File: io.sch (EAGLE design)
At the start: 53 parts, among them J1 SJ-3502-SMT-TR, Q1 2SCR574D3TL1, Q2 2SCR574D3TL1, U1 MCP1703T-5002E, U2 SA602AD8-SOIC, U3 LM386M-1, X1 Antenna, Y1 7.040MHz

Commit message: splitting boards, doing layouts
Split into two boards with jumpers between. Added jumper for crystal to be able to change reference frequency. Closer to real layouts, still need to solidify some parts.
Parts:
- removed C13: 47p, adafruit:C-USC0805
- removed C14: 220p, adafruit:C-USC0805
- removed C15: 0.1u, adafruit:C-USC0805
- removed C20, C21: 10n, adafruit:C-USC0805
- removed C26, C3: 33p, adafruit:C-USC0805
- removed C4: 270p, adafruit:C-USC0805
- removed D1, D2: 1N4148, adafruit:DIODE_SOD-123FL
- removed D3: MV2102, adafruit:DIODESOD-323F
- removed L1: 10uH, MLF2012E5R6KT000:MLF2012E5R6KT000
- removed L6: 18uH, MLF2012E5R6KT000:MLF2012E5R6KT000
- removed L7: 560uH, MLF2012E5R6KT000:MLF2012E5R6KT000
- removed L8: 5.6uH, MLF2012E5R6KT000:MLF2012E5R6KT000
- removed R1, R2: 1k, pot:TRIM_EU-3223G
- removed R3: 6.8k, adafruit:R-US_M0805
- removed U2: SA602AD8-SOIC, zort2:SA602AD8-SOIC
- removed VIN: AB9V, battery:AB9V
- removed Y1: 7.040MHz, adafruit:CRYSTALCTS406
- added JP1: (no value), adafruit:PINHD-2X4
- added U$2: 9V_968, zort2:9V_968
- L2: device MLF2012E5R6KT000:MLF2012E5R6KT000 -> Inductor:L_CHIP-1008(2520-METRIC)
- L4: device MLF2012E5R6KT000:MLF2012E5R6KT000 -> zort2:B966AS-160M-P3
- L5: device MLF2012E5R6KT000:MLF2012E5R6KT000 -> Inductor:L_CHIP-0805(2012-METRIC)
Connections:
- removed net N$1: C20.1, U2.IN_A
- removed net N$15: L6.2, Y1.1
- removed net N$16: C15.2, L6.1
- removed net N$17: C15.1, D3.C, L7.2
- removed net N$18: L7.1, R2.S
- removed net N$2: C21.1, U2.IN_B
- removed net N$3: C20.2, C26.1, C3.1, L1.2
- removed net N$4: C14.1, U2.OSC_B, Y1.2
- removed net N$5: C26.2, C3.2, C4.1, R1.S
- removed net N$6: L8.2, R1.E
- net 6V_DC: now also JP1.3; no longer R2.E, U2.VCC
- net ANT_IN: now also JP1.7; no longer D1.A, D2.C, L8.1
- net ANT_OUT: now also JP1.8; no longer C13.1, C14.2, R3.2, U2.OSC_E
- net GND: now also JP1.2, U$2.P$2; no longer C13.2, C21.2, C4.2, D1.C, D2.A, D3.A, L1.1, R1.A, R2.A, R3.1, U2.GND, VIN.-
- net OUT_A: now also JP1.5; no longer U2.OUT_A
- net OUT_B: now also JP1.6; no longer U2.OUT_B
- net VIN: now also JP1.1, U$2.P$1; no longer VIN.+
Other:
- note removed: "Input Attenuation"
- note removed: "RF Mixer"
- note removed: "VXO"
- moved on the sheet: C1, C10, C11, C12, C16, C17, C18, C19, C2, C22, C23, C24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

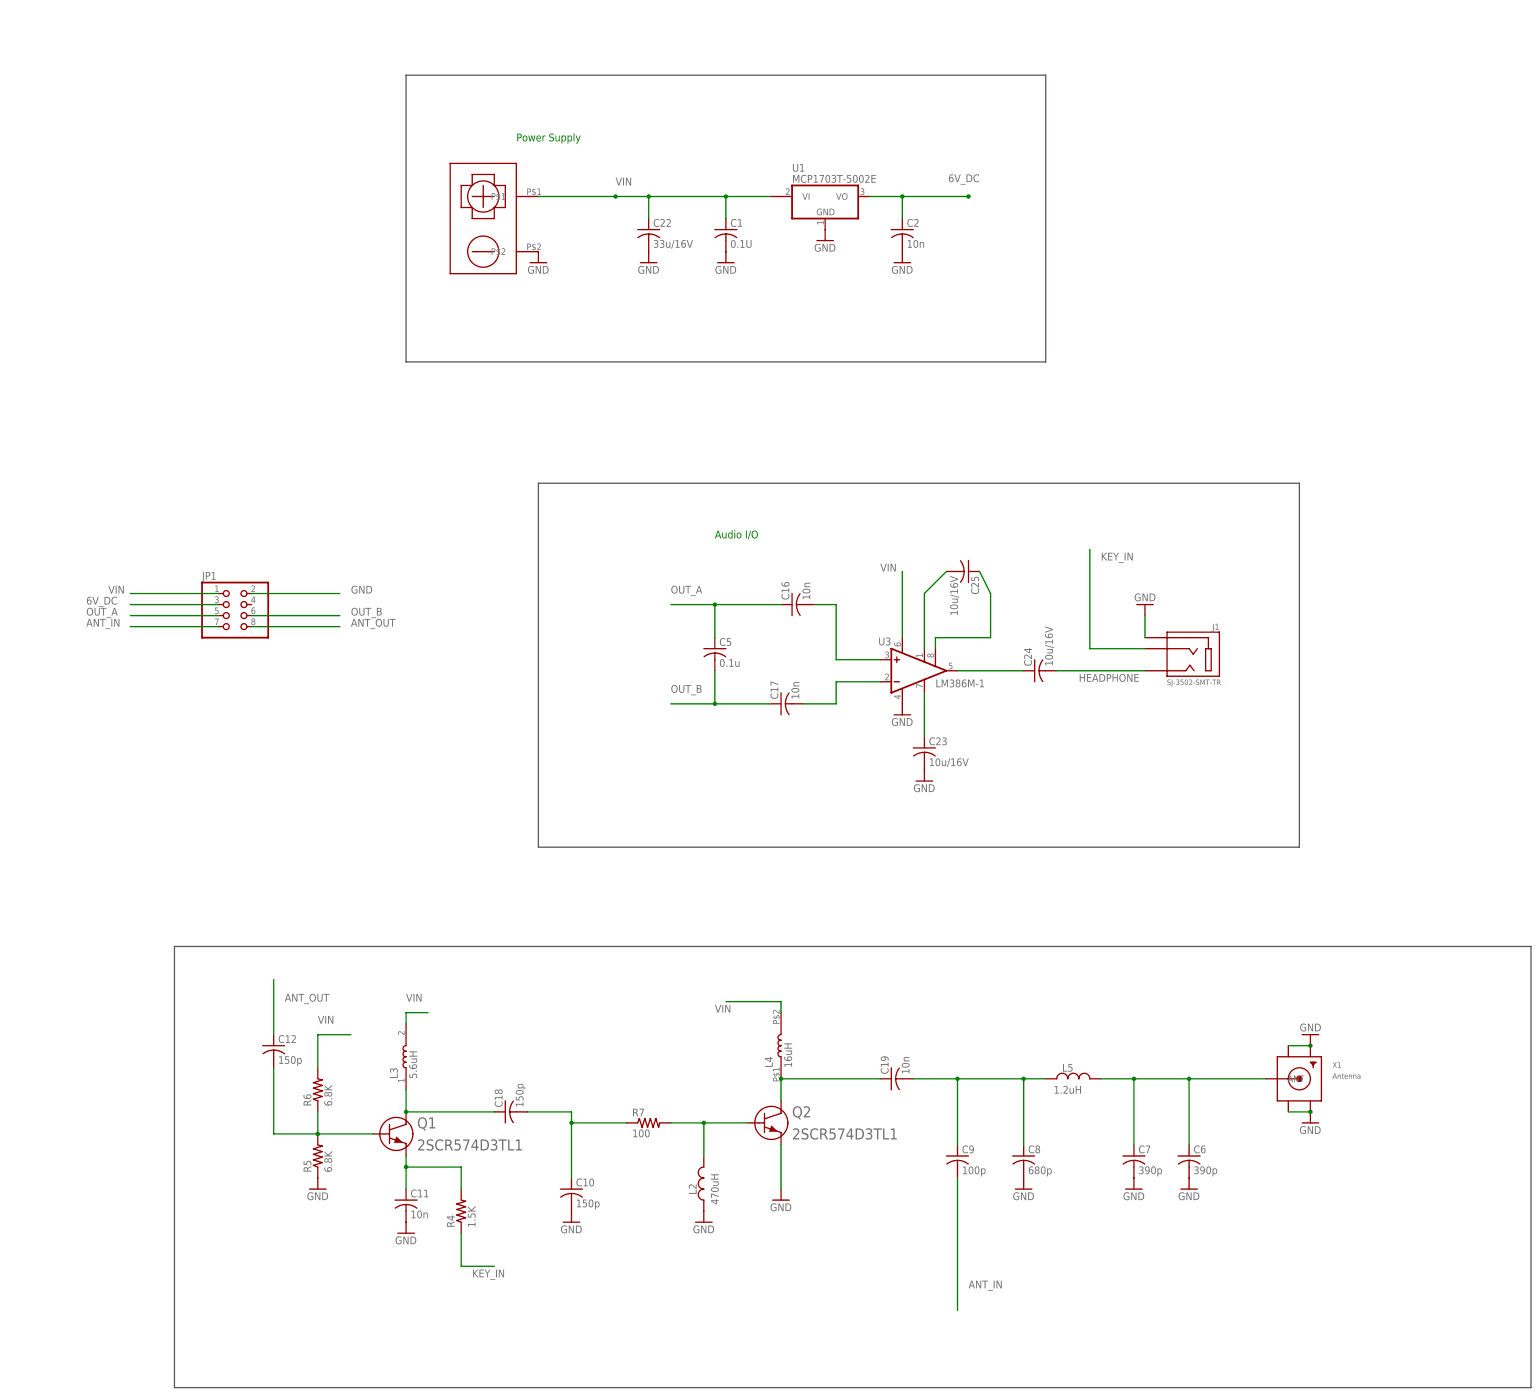
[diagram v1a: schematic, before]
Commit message: updated Q1, added readme
Updated Q1 to be a better replacement for the original PN2222A in an SMD format. Also added a readme, with links to PNGs of the schematics and layout renderings, as well as a photo of one of my prototypes.
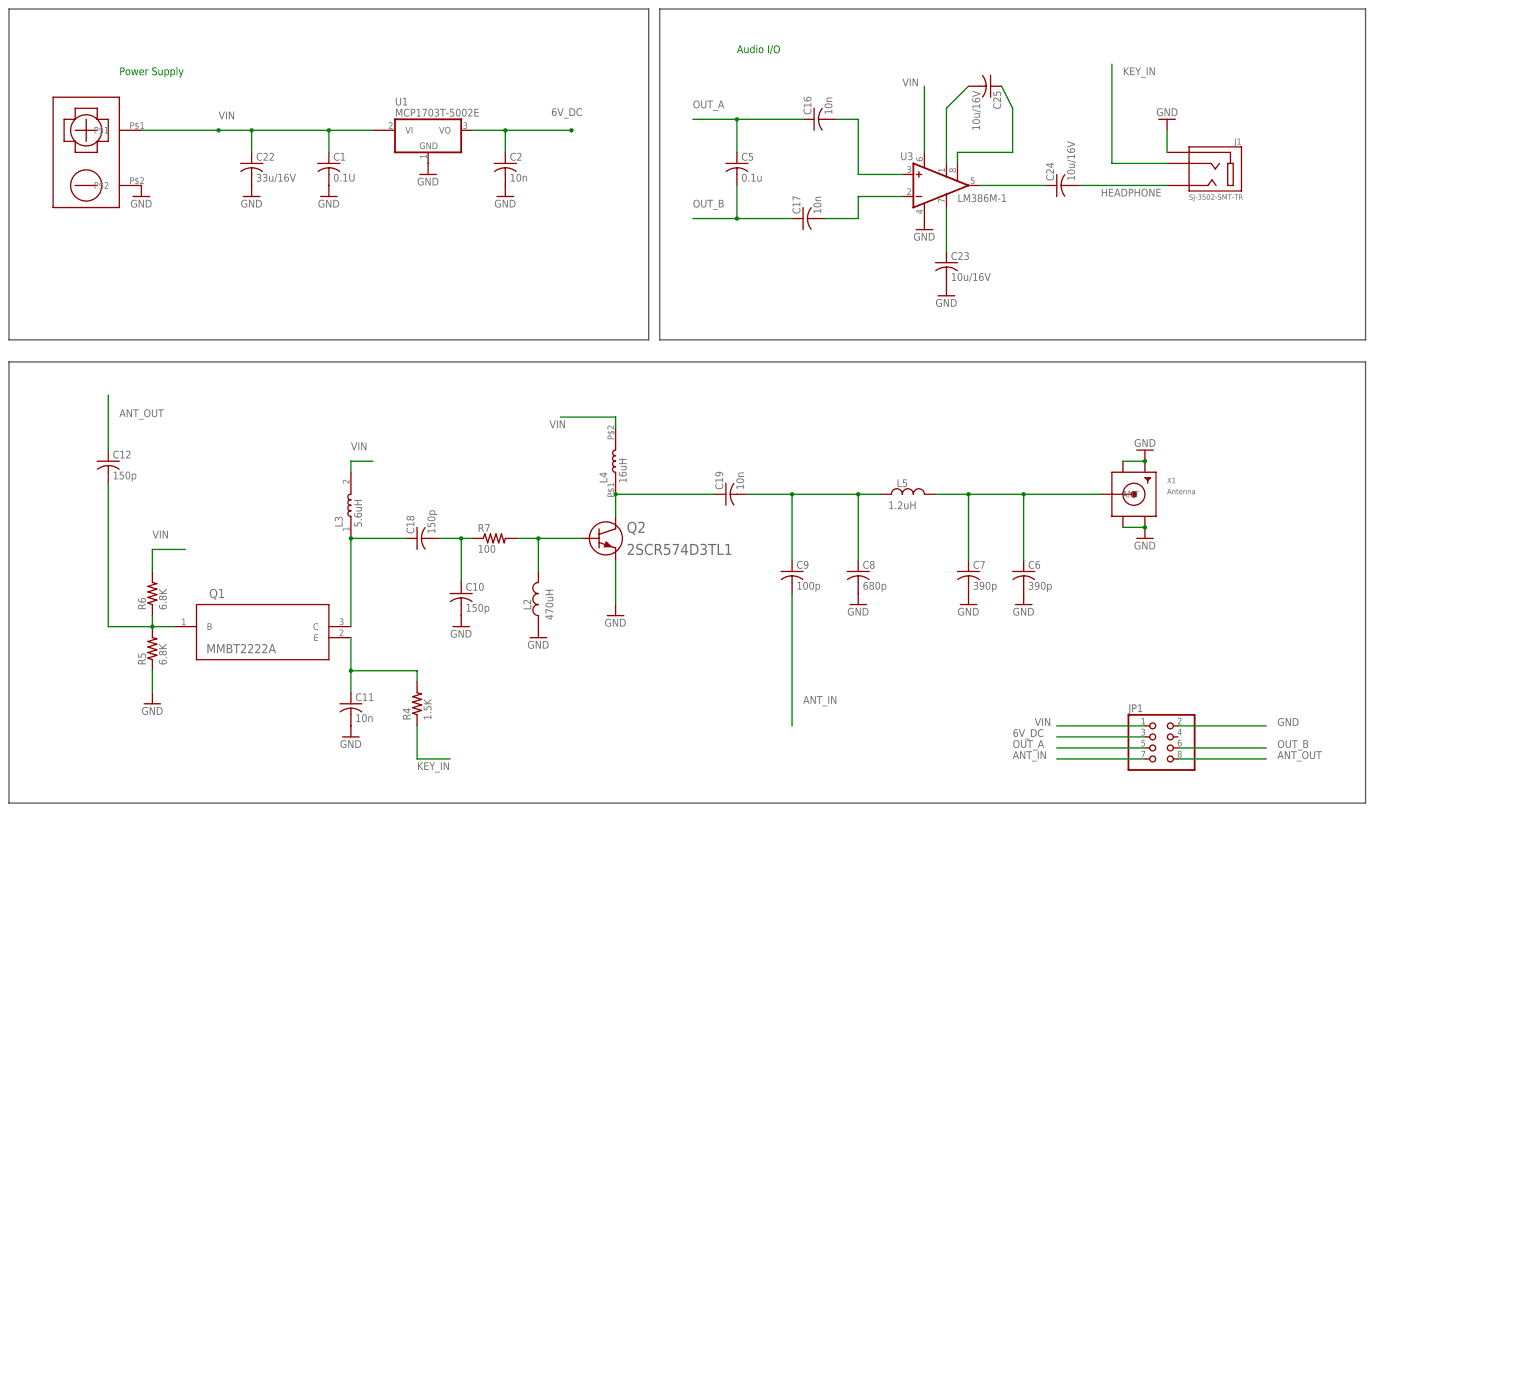
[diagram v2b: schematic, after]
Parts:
- Q1: value 2SCR574D3TL1 -> MMBT2222A; device zort2:2SCR574D3TL1 -> zort2:MMBT2222A-7-FSOT-23_DIO-M
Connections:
- net N$19: now also Q1.B; no longer Q1.1
- net N$20: now also Q1.E; no longer Q1.3
- net N$21: now also Q1.C; no longer Q1.2
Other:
- moved on the sheet: C1, C10, C11, C12, C16, C17, C18, C19, C2, C22, C23, C24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

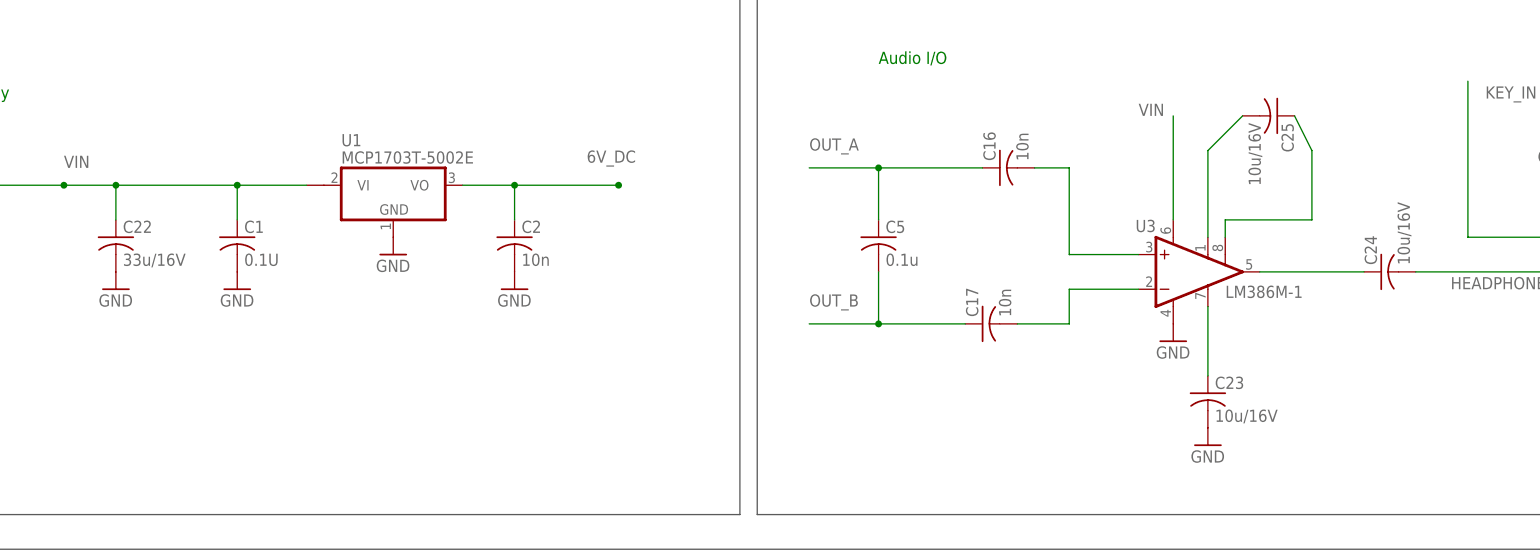
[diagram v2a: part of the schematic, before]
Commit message: cleaned up boards, new screenshots
Cleaned up the orientation and text on the boards. Ran them through the OshPark rules, and sent off v1 to get printed
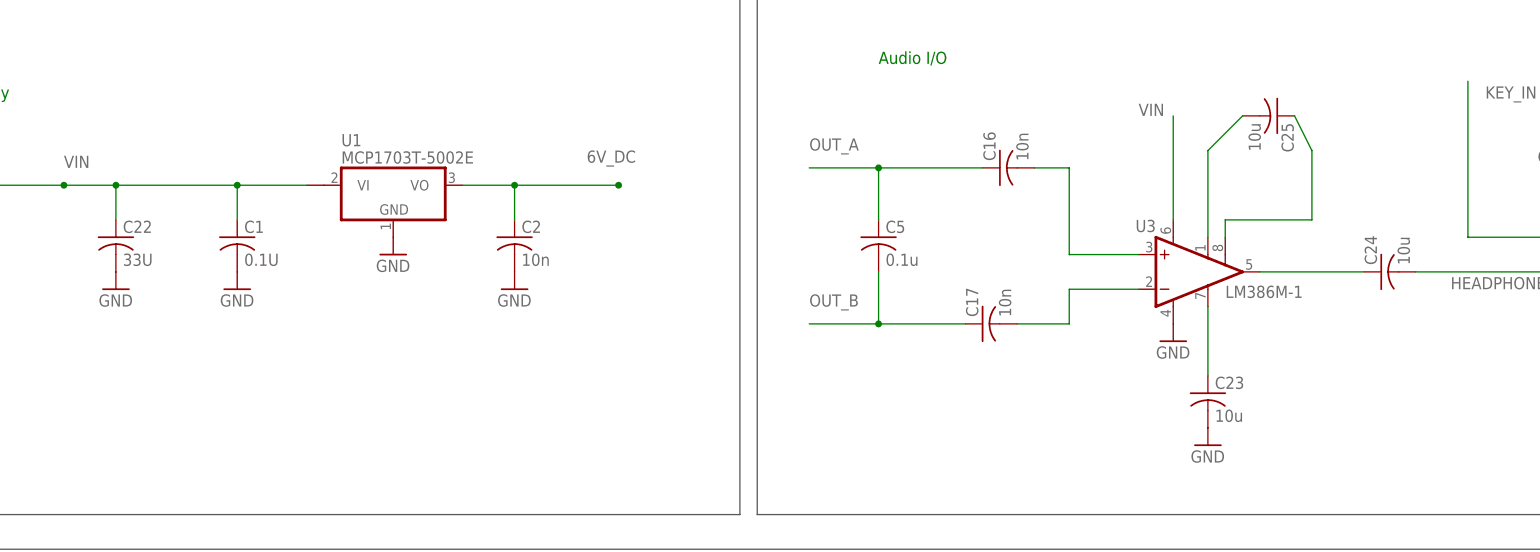
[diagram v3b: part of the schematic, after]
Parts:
- removed U$2: 9V_968, zort2:9V_968
- added U$1: 9V_9689V_968_SMD, zort2:9V_9689V_968_SMD
- C22: value 33u/16V -> 33U
- C23, C24, C25: value 10u/16V -> 10u
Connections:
- net GND: now also U$1.P$2; no longer U$2.P$2
- net VIN: now also U$1.P$1; no longer U$2.P$1
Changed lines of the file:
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@@
 <class number="0" name="default" width="0" drill="0">
+</class>
+<class number="1" name="power" width="0.3048" drill="0">
 </class>
 </classes>
 <parts>
-<part name="C22" library="adafruit" library_urn="urn:adsk.eagle:library:420" deviceset="C-US" device="C0805" package3d_urn="urn:adsk.eagle:package:6240337/1" value="33u/16V"/>
+<part name="C22" library="adafruit" library_urn="urn:adsk.eagle:library:420" deviceset="C-US" device="C0805" package3d_urn="urn:adsk.eagle:package:6240337/1" value="33U"/>
 <part name="C1" library="adafruit" library_urn="urn:adsk.eagle:library:420" deviceset="C-US" device="C0805" package3d_urn="urn:adsk.eagle:package:6240337/1" value="0.1U"/>
 <part name="C2" library="adafruit" library_urn="urn:adsk.eagle:library:420" deviceset="C-US" device="C0805" package3d_urn="urn:adsk.eagle:package:6240337/1" value="10n"/>
@@
 <part name="C16" library="adafruit" library_urn="urn:adsk.eagle:library:420" deviceset="C-US" device="C0805" package3d_urn="urn:adsk.eagle:package:6240337/1" value="10n"/>
 <part name="C17" library="adafruit" library_urn="urn:adsk.eagle:library:420" deviceset="C-US" device="C0805" package3d_urn="urn:adsk.eagle:package:6240337/1" value="10n"/>
-<part name="C23" library="adafruit" library_urn="urn:adsk.eagle:library:420" deviceset="C-US" device="C0805" package3d_urn="urn:adsk.eagle:package:6240337/1" value="10u/16V"/>
-<part name="C25" library="adafruit" library_urn="urn:adsk.eagle:library:420" deviceset="C-US" device="C0805" package3d_urn="urn:adsk.eagle:package:6240337/1" value="10u/16V"/>
-<part name="C24" library="adafruit" library_urn="urn:adsk.eagle:library:420" deviceset="C-US" device="C0805" package3d_urn="urn:adsk.eagle:package:6240337/1" value="10u/16V"/>
+<part name="C23" library="adafruit" library_urn="urn:adsk.eagle:library:420" deviceset="C-US" device="C0805" package3d_urn="urn:adsk.eagle:package:6240337/1" value="10u"/>
+<part name="C25" library="adafruit" library_urn="urn:adsk.eagle:library:420" deviceset="C-US" device="C0805" package3d_urn="urn:adsk.eagle:package:6240337/1" value="10u"/>
+<part name="C24" library="adafruit" library_urn="urn:adsk.eagle:library:420" deviceset="C-US" device="C0805" package3d_urn="urn:adsk.eagle:package:6240337/1" value="10u"/>
 <part name="U3" library="linear" library_urn="urn:adsk.eagle:library:262" deviceset="LM386?-*" device="M" package3d_urn="urn:adsk.eagle:package:16404/2" technology="1"/>
 <part name="GND8" library="supply1" library_urn="urn:adsk.eagle:library:371" deviceset="GND" device=""/>
@@
 <part name="L4" library="zort2" deviceset="B966AS-160M-P3" device="" value="16uH"/>
 <part name="L2" library="Inductor" library_urn="urn:adsk.eagle:library:16378440" deviceset="L" device="CHIP-1008(2520-METRIC)" package3d_urn="urn:adsk.eagle:package:16378469/1" technology="_" value="470uH"/>
-<part name="U$2" library="zort2" deviceset="9V_968" device=""/>
 <part name="Q2" library="zort2" deviceset="2SCR574D3TL1" device=""/>
 <part name="Q1" library="zort2" deviceset="MMBT2222A-7-F" device="SOT-23_DIO-M" value="MMBT2222A"/>
+<part name="U$1" library="zort2" deviceset="9V_968" device="9V_968_SMD"/>
 </parts>
 <sheets>
@@
 <attribute name="VALUE" x="27.94" y="-15.24" size="1.778" layer="96" rot="R90" align="center"/>
 </instance>
-<instance part="U$2" gate="G$1" x="-78.74" y="88.9" smashed="yes"/>
 <instance part="Q2" gate="A" x="40.64" y="0" smashed="yes">
 <attribute name="NAME" x="45.72" y="1.27" size="2.54" layer="95" ratio="10" rot="SR0"/>
@@
 <attribute name="VALUE" x="-51.0794" y="-26.4414" size="2.0828" layer="96" ratio="6" rot="SR0"/>
 </instance>
+<instance part="U$1" gate="G$1" x="-78.74" y="88.9" smashed="yes"/>
 </instances>
 <busses>
 </busses>
 <nets>
-<net name="VIN" class="0">
+<net name="VIN" class="1">
 <segment>
 <wire x1="-66.04" y1="93.98" x2="-48.26" y2="93.98" width="0.1524" layer="91"/>
@@
 <pinref part="U1" gate="G$1" pin="VI1"/>
 <wire x1="-22.86" y1="93.98" x2="-12.7" y2="93.98" width="0.1524" layer="91"/>
-<pinref part="U$2" gate="G$1" pin="P$1"/>
+<pinref part="U$1" gate="G$1" pin="P$1"/>
 </segment>
 <segment>
@@
 </segment>
 <segment>
-<pinref part="U$2" gate="G$1" pin="P$2"/>
 <pinref part="GND1" gate="1" pin="GND"/>
+<pinref part="U$1" gate="G$1" pin="P$2"/>
 </segment>
 </net>
